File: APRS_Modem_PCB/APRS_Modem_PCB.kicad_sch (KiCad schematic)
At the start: 36 parts, among them Q1 2N3904, Q2 2N3904, Q3 2N3904

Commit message: start PCB
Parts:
- removed Q3: 2N3904, Package_TO_SOT_THT:TO-92_Inline, symbol Transistor_BJT:2N3904
- added C2: 0.1uF, Capacitor_THT:C_Disc_D4.3mm_W1.9mm_P5.00mm, symbol Device:C
- added J1, J2: Conn_02x10_Odd_Even, Connector_PinHeader_2.54mm:PinHeader_2x10_P2.54mm_Vertical, symbol Connector_Generic:Conn_02x10_Odd_Even
- added R14, R22: 10k, Resistor_THT:R_Axial_DIN0207_L6.3mm_D2.5mm_P10.16mm_Horizontal, symbol Device:R_US
- added R23: 8.2k, Resistor_THT:R_Axial_DIN0207_L6.3mm_D2.5mm_P10.16mm_Horizontal, symbol Device:R_US
- added R24: 2.2k, Resistor_THT:R_Axial_DIN0207_L6.3mm_D2.5mm_P10.16mm_Horizontal, symbol Device:R_US
- added R25: 560, Resistor_THT:R_Axial_DIN0207_L6.3mm_D2.5mm_P10.16mm_Horizontal, symbol Device:R_US
- added U1: LM741, Package_DIP:DIP-8_W7.62mm_LongPads, symbol Amplifier_Operational:LM741
- C1, C5: footprint (none) -> Capacitor_THT:CP_Radial_D8.0mm_P3.80mm
- C3, C4: footprint (none) -> Capacitor_THT:C_Disc_D4.3mm_W1.9mm_P5.00mm
- C6: value 0.1uF -> 100uF; footprint (none) -> Capacitor_THT:CP_Radial_D8.0mm_P3.80mm
- C7: value 100uF -> 0.1uF; footprint (none) -> Capacitor_THT:C_Disc_D4.3mm_W1.9mm_P5.00mm
- D1, D2, D3, D4: footprint (none) -> Diode_THT:D_A-405_P7.62mm_Horizontal
- MIC1, SPKR1: footprint (none) -> Connector_Audio:Jack_3.5mm_CUI_SJ1-3525N_Horizontal
- R1, R10, R13, R4, R6: footprint (none) -> Resistor_THT:R_Axial_DIN0207_L6.3mm_D2.5mm_P5.08mm_Vertical
- R11, R16, R17, R18, R2, R8: footprint (none) -> Resistor_THT:R_Axial_DIN0207_L6.3mm_D2.5mm_P10.16mm_Horizontal
- R12: value 8.2k -> 10k; footprint (none) -> Resistor_THT:R_Axial_DIN0207_L6.3mm_D2.5mm_P5.08mm_Vertical
- R15: value 330 -> 2.2k; footprint (none) -> Resistor_THT:R_Axial_DIN0207_L6.3mm_D2.5mm_P10.16mm_Horizontal
- R19: value 8.2k -> 330; footprint (none) -> Resistor_THT:R_Axial_DIN0207_L6.3mm_D2.5mm_P10.16mm_Horizontal
- R20: value 2.2k -> 10k; footprint (none) -> Resistor_THT:R_Axial_DIN0207_L6.3mm_D2.5mm_P10.16mm_Horizontal
- R21: value 560 -> 1k; footprint (none) -> Resistor_THT:R_Axial_DIN0207_L6.3mm_D2.5mm_P10.16mm_Horizontal
- R3, R7, R9: value 5k -> 10k; footprint (none) -> Resistor_THT:R_Axial_DIN0207_L6.3mm_D2.5mm_P5.08mm_Vertical
- R5: value 5k -> 10k; footprint (none) -> Resistor_THT:R_Axial_DIN0207_L6.3mm_D2.5mm_P10.16mm_Horizontal
- RV1: footprint (none) -> Potentiometer_THT:Potentiometer_Alpha_RD901F-40-00D_Single_Vertical
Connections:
- net +3V3: now also J1.1 (Pin_1), R22.1; no longer R18.1
- net +5V: now also R17.1, C2.1, J1.2 (Pin_2), U1.7 (V+); no longer R11.1
- net ADC_IN: now also R21.1, J1.3 (Pin_3); no longer R17.1
- net DAC_0: now also J2.3 (Pin_3)
- net DAC_1: now also R5.2, J2.5 (Pin_5); no longer R4.2
- net DAC_2: now also R8.2, J2.7 (Pin_7); no longer R6.2
- net DAC_3: now also R11.2, J2.9 (Pin_9); no longer R8.2
- net DAC_4: now also J2.11 (Pin_11), R14.2; no longer R10.2
- net GND: now also C7.2, R18.2, R20.2, R21.2, C2.2, J1.4 (Pin_4), R23.2, U1.4 (V-); no longer C6.2, R12.2, R13.2, R17.2, R19.2
- net PTT: now also J1.20 (Pin_20), R24.1; no longer R20.1
- net at R6.1, R7.1: now also R3.2, R4.2, R5.1; no longer R5.2
- net at R7.2, R8.1, R9.1: now also R10.1, R6.2
- net at R13.1: now also R10.2, R11.1, R12.1, R9.2; no longer R15.1
- net at R1.1, R2.1, R3.1: now also R4.1
- net at D1.2 (K), D3.1 (A), SPKR1.T: now also C6.2; no longer C7.2
- net at MIC1.R: now also R25.2; no longer R21.2
- net at MIC1.S, Q2.3 (C): now also C7.1; no longer C6.1
- net at C3.1, C4.1: now also R19.2; no longer R15.2
- net at C4.2, RV1.1: now also R20.1; no longer R16.1
- net at C5.2: now also R25.1; no longer R21.1
- net at Q2.2 (B): now also R24.2; no longer R20.2
- new net: R12.2, R13.2, R14.1, R15.1
- new net: C6.1, Q1.2 (B), R22.2, R23.1
- new net: R19.1, U1.2 (-), U1.6
- new net: C1.2, R17.2, R18.1, U1.3 (+)
- new net: C1.1, R15.2, R16.1
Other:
- moved on the sheet: R1

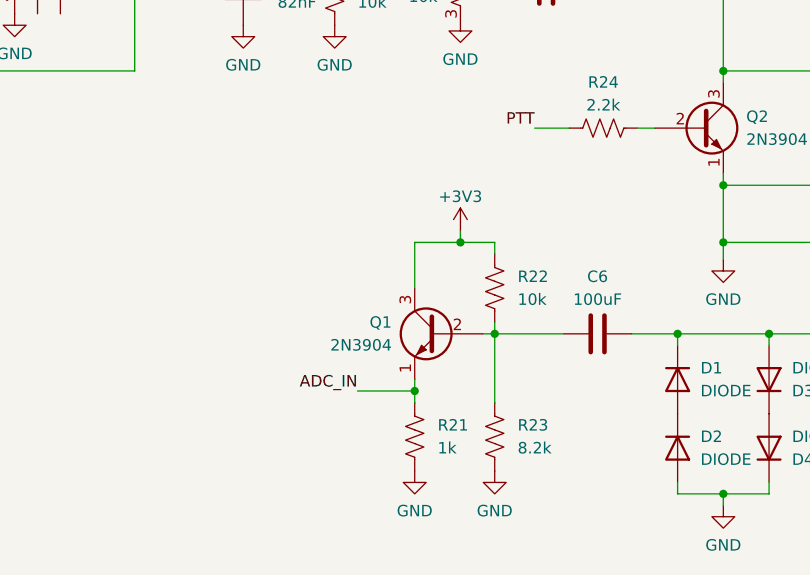
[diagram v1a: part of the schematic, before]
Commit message: update schematic
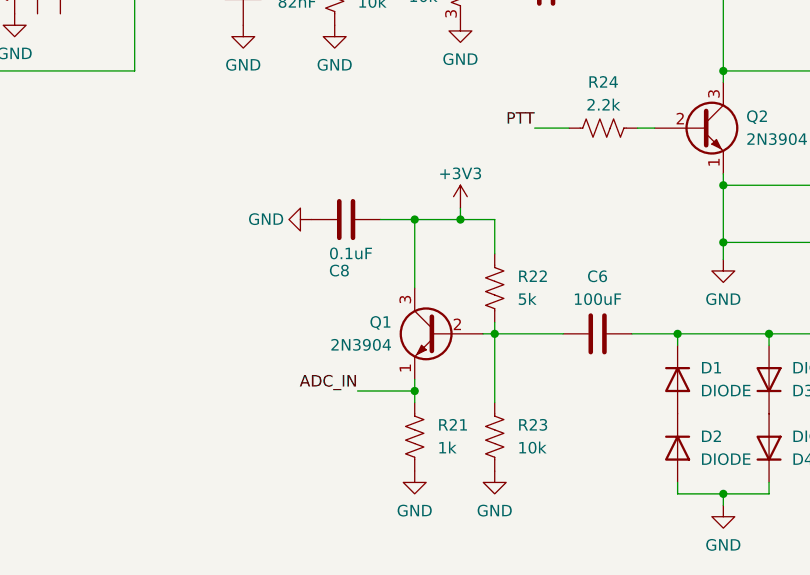
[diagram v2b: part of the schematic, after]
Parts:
- added C8: 0.1uF, Capacitor_THT:C_Disc_D4.3mm_W1.9mm_P5.00mm, symbol Device:C
- R22: value 10k -> 5k
- R23: value 8.2k -> 10k
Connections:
- net +3V3: now also C8.1
- net GND: now also C8.2
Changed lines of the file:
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@@
   (junction (at 209.55 132.08) (diameter 0) (color 0 0 0 0)
   )
+  (junction (at 175.26 101.6) (diameter 0) (color 0 0 0 0)
+  )
   (junction (at 87.63 60.325) (diameter 0) (color 0 0 0 0)
   )
-  (junction (at 180.34 104.14) (diameter 0) (color 0 0 0 0)
+  (junction (at 180.34 101.6) (diameter 0) (color 0 0 0 0)
   )
   (junction (at 144.145 71.12) (diameter 0) (color 0 0 0 0)
@@
     (stroke (width 0) (type default) (color 0 0 0 0))
   )
-  (wire (pts (xy 184.15 105.41) (xy 184.15 104.14))
+  (wire (pts (xy 184.15 105.41) (xy 184.15 101.6))
     (stroke (width 0) (type default) (color 0 0 0 0))
   )
@@
     (stroke (width 0) (type default) (color 0 0 0 0))
   )
-  (wire (pts (xy 175.26 104.14) (xy 180.34 104.14))
+  (wire (pts (xy 175.26 101.6) (xy 180.34 101.6))
     (stroke (width 0) (type default) (color 0 0 0 0))
   )
@@
     (stroke (width 0) (type default) (color 0 0 0 0))
   )
-  (wire (pts (xy 180.34 104.14) (xy 184.15 104.14))
+  (wire (pts (xy 180.34 101.6) (xy 184.15 101.6))
     (stroke (width 0) (type default) (color 0 0 0 0))
   )
@@
     (stroke (width 0) (type default) (color 0 0 0 0))
   )
-  (wire (pts (xy 180.34 102.87) (xy 180.34 104.14))
+  (wire (pts (xy 180.34 100.33) (xy 180.34 101.6))
     (stroke (width 0) (type default) (color 0 0 0 0))
   )
@@
     (stroke (width 0) (type default) (color 0 0 0 0))
   )
-  (wire (pts (xy 175.26 109.22) (xy 175.26 104.14))
+  (wire (pts (xy 175.26 109.22) (xy 175.26 101.6))
     (stroke (width 0) (type default) (color 0 0 0 0))
   )
@@
   )
   (wire (pts (xy 123.19 73.66) (xy 125.73 73.66))
+    (stroke (width 0) (type default) (color 0 0 0 0))
+  )
+  (wire (pts (xy 171.45 101.6) (xy 175.26 101.6))
     (stroke (width 0) (type default) (color 0 0 0 0))
   )
@@
       (effects (font (size 1.27 1.27)) (justify left))
     )
-    (property "Value" "10k" (id 1) (at 186.69 110.4899 0)
+    (property "Value" "5k" (id 1) (at 186.69 110.4899 0)
       (effects (font (size 1.27 1.27)) (justify left))
     )
@@
       (effects (font (size 1.27 1.27)) (justify left))
     )
-    (property "Value" "8.2k" (id 1) (at 186.69 126.9999 0)
+    (property "Value" "10k" (id 1) (at 186.69 126.9999 0)
       (effects (font (size 1.27 1.27)) (justify left))
     )
@@
     (pin "1")
     (pin "2")
+  )
+  (symbol (lib_id "power:GND") (at 163.83 101.6 270) (unit 1)
+    (in_bom yes) (on_board yes)
+    (property "Reference" "#PWR019" (id 0) (at 157.48 101.6 0)
+      (effects (font (size 1.27 1.27)) hide)
+    )
+    (property "Value" "GND" (id 1) (at 158.75 101.6 90))
+    (property "Footprint" "" (id 2) (at 163.83 101.6 0)
+      (effects (font (size 1.27 1.27)) hide)
+    )
+    (property "Datasheet" "" (id 3) (at 163.83 101.6 0)
+      (effects (font (size 1.27 1.27)) hide)
+    )
+    (pin "1")
   )
   (symbol (lib_id "power:GND") (at 180.34 79.375 0) (unit 1)
@@
     (pin "3")
   )
-  (symbol (lib_id "power:+3V3") (at 180.34 102.87 0) (unit 1)
+  (symbol (lib_id "power:+3V3") (at 180.34 100.33 0) (unit 1)
     (in_bom yes) (on_board yes)
-    (property "Reference" "#PWR015" (id 0) (at 180.34 106.68 0)
-      (effects (font (size 1.27 1.27)) hide)
-    )
-    (property "Value" "+3V3" (id 1) (at 180.34 99.06 0))
-    (property "Footprint" "" (id 2) (at 180.34 102.87 0)
-      (effects (font (size 1.27 1.27)) hide)
-    )
-    (property "Datasheet" "" (id 3) (at 180.34 102.87 0)
+    (property "Reference" "#PWR015" (id 0) (at 180.34 104.14 0)
+      (effects (font (size 1.27 1.27)) hide)
+    )
+    (property "Value" "+3V3" (id 1) (at 180.34 96.52 0))
+    (property "Footprint" "" (id 2) (at 180.34 100.33 0)
+      (effects (font (size 1.27 1.27)) hide)
+    )
+    (property "Datasheet" "" (id 3) (at 180.34 100.33 0)
       (effects (font (size 1.27 1.27)) hide)
     )
@@
     )
     (pin "1")
+  )
+  (symbol (lib_id "Device:C") (at 167.64 101.6 270) (unit 1)
+    (in_bom yes) (on_board yes)
+    (property "Reference" "C8" (id 0) (at 165.735 107.315 90)
+      (effects (font (size 1.27 1.27)) (justify left))
+    )
+    (property "Value" "0.1uF" (id 1) (at 165.735 105.41 90)
+      (effects (font (size 1.27 1.27)) (justify left))
+    )
+    (property "Footprint" "Capacitor_THT:C_Disc_D4.3mm_W1.9mm_P5.00mm" (id 2) (at 163.83 102.5652 0)
+      (effects (font (size 1.27 1.27)) hide)
+    )
+    (property "Datasheet" "~" (id 3) (at 167.64 101.6 0)
+      (effects (font (size 1.27 1.27)) hide)
+    )
+    (pin "1")
+    (pin "2")
   )
   (symbol (lib_id "power:GND") (at 130.81 78.74 0) (unit 1)
@@
       (reference "#PWR018") (unit 1) (value "GND") (footprint "")
     )
+    (path "/9d584a70-1339-4817-aae7-3adf7dfd407d"
+      (reference "#PWR019") (unit 1) (value "GND") (footprint "")
+    )
     (path "/9caf7065-7471-44fc-b5bd-21c7e67d6596"
       (reference "C1") (unit 1) (value "100uF") (footprint "Capacitor_THT:CP_Radial_D8.0mm_P3.80mm")
@@
       (reference "C7") (unit 1) (value "0.1uF") (footprint "Capacitor_THT:C_Disc_D4.3mm_W1.9mm_P5.00mm")
     )
+    (path "/f10ff713-e47f-4fb3-aca4-3df831c42b13"
+      (reference "C8") (unit 1) (value "0.1uF") (footprint "Capacitor_THT:C_Disc_D4.3mm_W1.9mm_P5.00mm")
+    )
     (path "/72fcdaa5-1edb-4d3e-a6cd-8796df0b8d03"
       (reference "D1") (unit 1) (value "DIODE") (footprint "Diode_THT:D_A-405_P7.62mm_Horizontal")
@@
     )
     (path "/18b1b0c5-17eb-4d22-b87e-a121730a1af2"
-      (reference "R22") (unit 1) (value "10k") (footprint "Resistor_THT:R_Axial_DIN0207_L6.3mm_D2.5mm_P10.16mm_Horizontal")
+      (reference "R22") (unit 1) (value "5k") (footprint "Resistor_THT:R_Axial_DIN0207_L6.3mm_D2.5mm_P10.16mm_Horizontal")
     )
     (path "/69d782a4-fd6d-4de8-86d9-6c6845f77b44"
-      (reference "R23") (unit 1) (value "8.2k") (footprint "Resistor_THT:R_Axial_DIN0207_L6.3mm_D2.5mm_P10.16mm_Horizontal")
+      (reference "R23") (unit 1) (value "10k") (footprint "Resistor_THT:R_Axial_DIN0207_L6.3mm_D2.5mm_P10.16mm_Horizontal")
     )
     (path "/0af82e25-1050-4cf9-ba20-20f807a7c5d0"
